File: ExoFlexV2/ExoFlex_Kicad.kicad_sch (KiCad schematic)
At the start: 25 parts, among them J1 ScrewT+12V, J19 CN9, J2 ScrewT5V, J20 CN10, J3 ScrewTGND, J4 ScrewT12V, J5 ScrewT-12v, J6 CN7, J7 CN8, M1 MOT_EV(12V 9.2A), M2 MOT_DOR(12V 9.2A), P1 Conn_WallPlug, U2 ON/OFF_SW(20A), U3 SECU_BUT(20A)

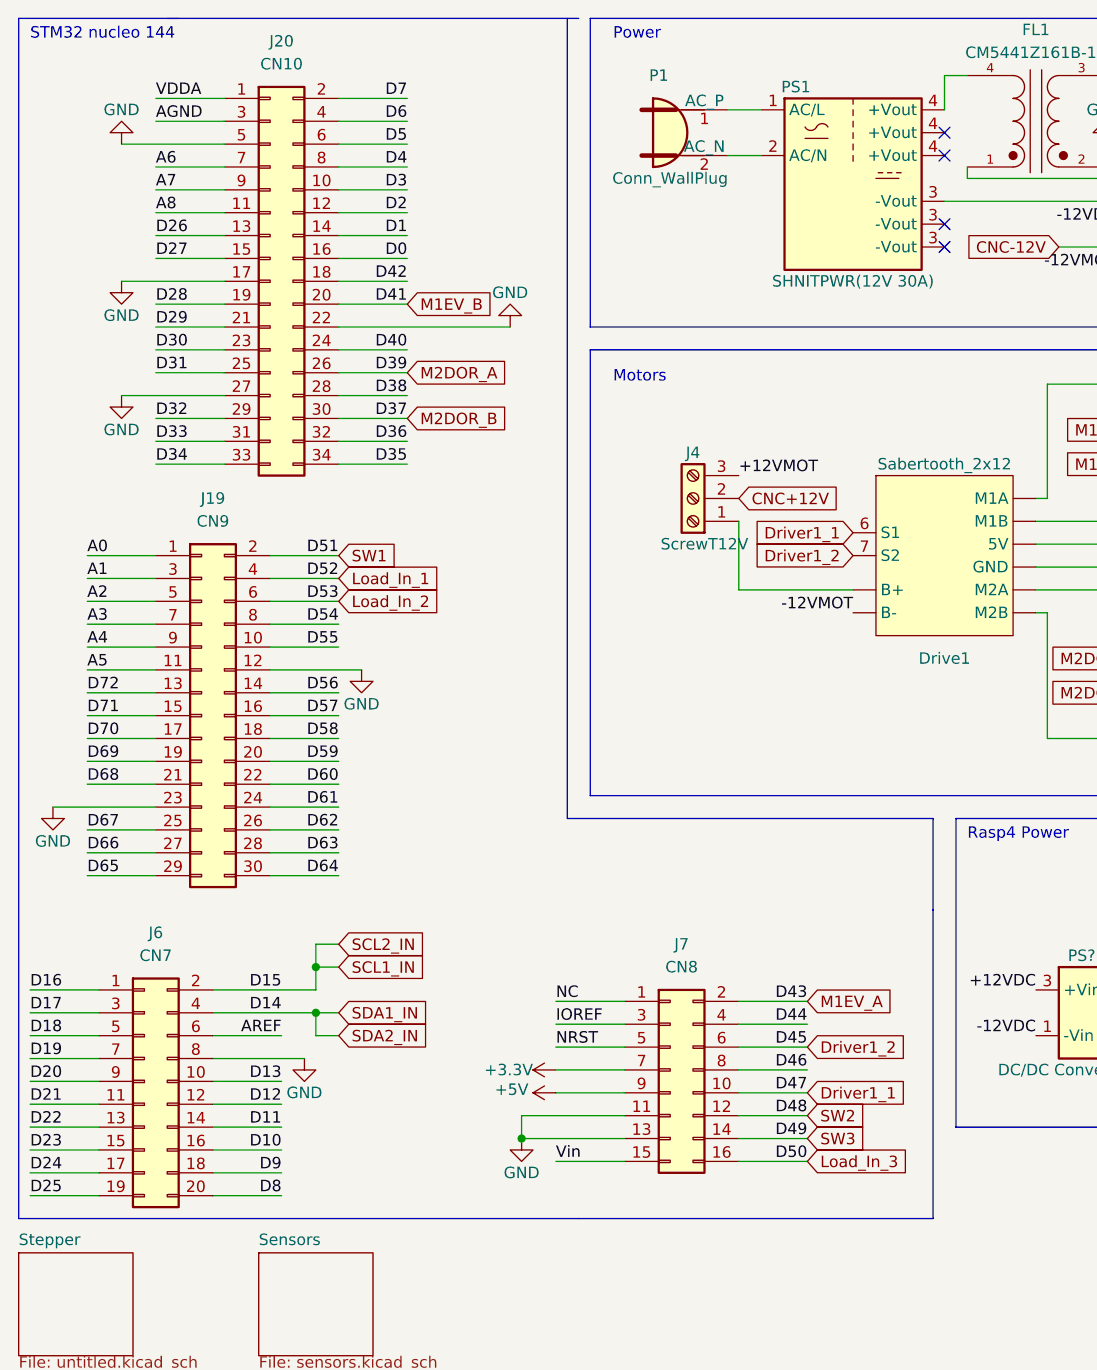
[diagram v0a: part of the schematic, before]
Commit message: Ajout des capteurs de courant, loadcell et potentiomètre et remplacement du stm32 par Raspberry Pi 4
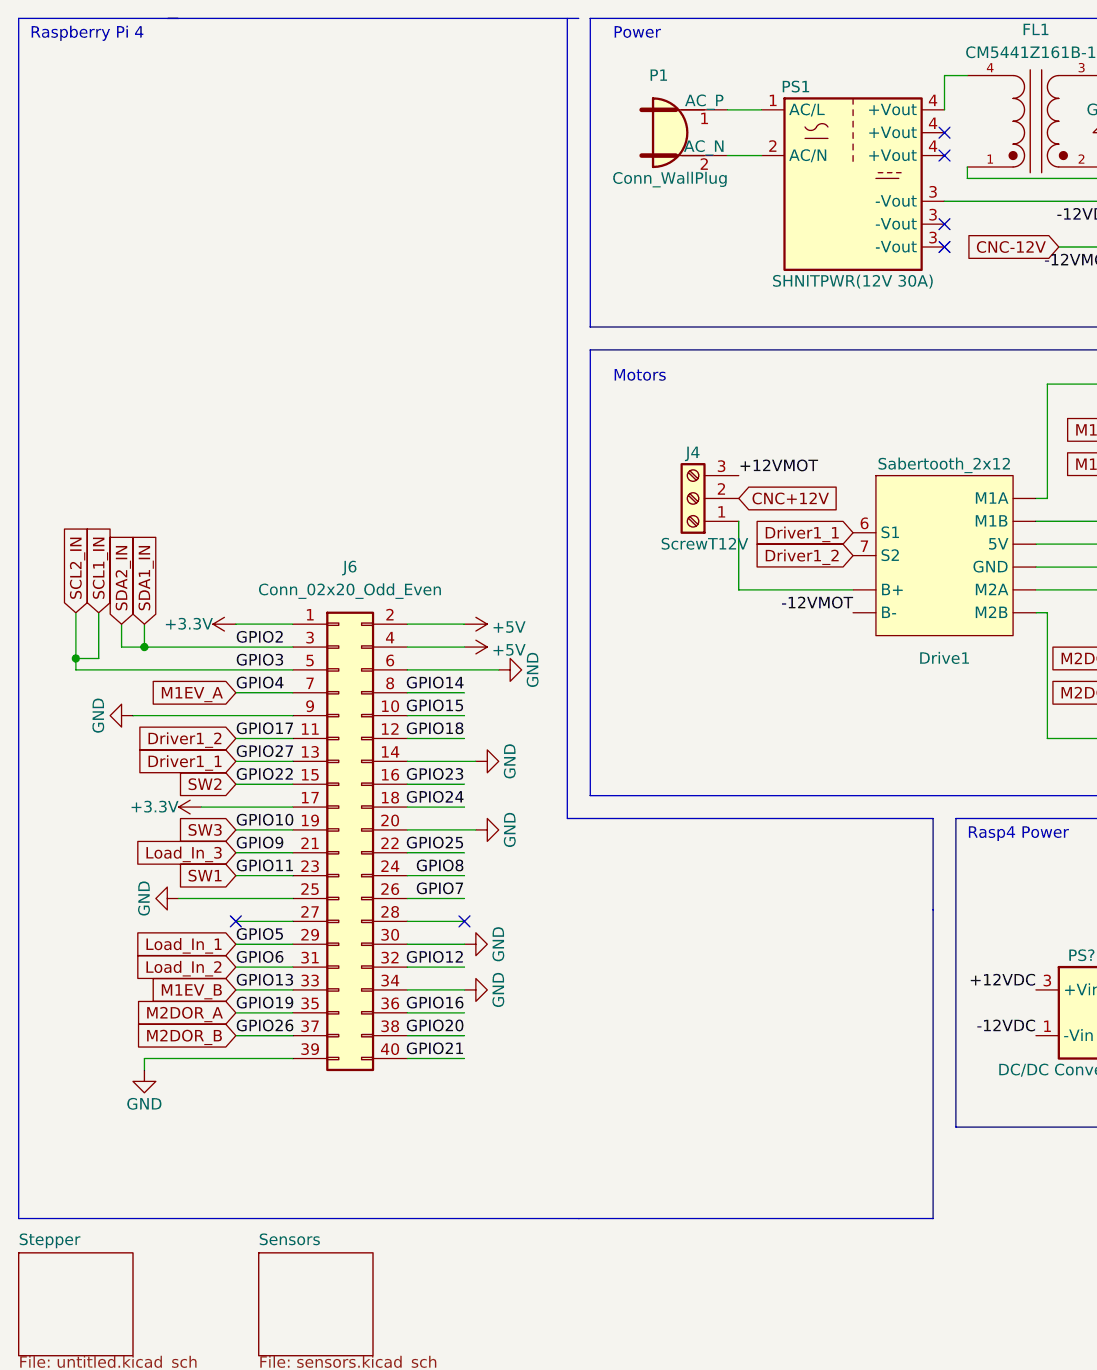
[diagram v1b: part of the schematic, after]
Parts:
- removed J19: CN9, Connector_PinSocket_2.54mm:PinSocket_2x15_P2.54mm_Vertical, symbol Connector_Generic:Conn_02x15_Odd_Even
- removed J20: CN10, Connector_PinSocket_2.54mm:PinSocket_2x17_P2.54mm_Vertical, symbol Connector_Generic:Conn_02x17_Odd_Even
- removed J6: CN7, Connector_PinSocket_2.54mm:PinSocket_2x10_P2.54mm_Vertical, symbol Connector_Generic:Conn_02x10_Odd_Even
- removed J7: CN8, Connector_PinSocket_2.54mm:PinSocket_2x08_P2.54mm_Vertical, symbol Connector_Generic:Conn_02x08_Odd_Even
- added J6: Conn_02x20_Odd_Even, symbol Connector_Generic:Conn_02x20_Odd_Even
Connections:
- net +3V3: now also J6.1 (Pin_1), J6.17 (Pin_17)
- net +5V: now also J6.2 (Pin_2), J6.4 (Pin_4)
- net Driver1_1: now also J6.13 (Pin_13)
- net Driver1_2: now also J6.11 (Pin_11)
- net GND: now also J6.14 (Pin_14), J6.20 (Pin_20), J6.25 (Pin_25), J6.30 (Pin_30), J6.34 (Pin_34), J6.39 (Pin_39), J6.6 (Pin_6), J6.9 (Pin_9)
- net Load_In_1: now also J6.29 (Pin_29)
- net Load_In_2: now also J6.31 (Pin_31)
- net Load_In_3: now also J6.21 (Pin_21)
- net M1EV_A: now also J6.7 (Pin_7)
- net M1EV_B: now also J6.33 (Pin_33)
- net M2DOR_A: now also J6.35 (Pin_35)
- net M2DOR_B: now also J6.37 (Pin_37)
- net SCL1_IN: now also J6.5 (Pin_5)
- net SDA1_IN: now also J6.3 (Pin_3)
- net SW1: now also J6.23 (Pin_23)
- net SW2: now also J6.15 (Pin_15)
- net SW3: now also J6.19 (Pin_19)
- net at PS1.3 (-Vout): now also J5.1 (Pin_1)
- net at PS1.4 (+Vout): now also FL1.4
- net at P?.S1 (Data_1): now also U?.3
- net at P?.S2 (Data_2): now also PS?.4 (-Vout)
- new net GPIO12: J6.32 (Pin_32)
- new net GPIO14: J6.8 (Pin_8)
- new net GPIO15: J6.10 (Pin_10)
- new net GPIO16: J6.36 (Pin_36)
- new net GPIO18: J6.12 (Pin_12)
- new net GPIO20: J6.38 (Pin_38)
- new net GPIO21: J6.40 (Pin_40)
- new net GPIO23: J6.16 (Pin_16)
- new net GPIO24: J6.18 (Pin_18)
- new net GPIO25: J6.22 (Pin_22)
- new net GPIO7: J6.26 (Pin_26)
- new net GPIO8: J6.24 (Pin_24)
- no-connect marks 8 -> 10
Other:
- note added: "Raspberry Pi 4"
- note removed: "STM32 nucleo 144"

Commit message: Backup du stm32
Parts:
- added J19: CN9, Connector_PinSocket_2.54mm:PinSocket_2x15_P2.54mm_Vertical, symbol Connector_Generic:Conn_02x15_Odd_Even
- added J20: CN10, Connector_PinSocket_2.54mm:PinSocket_2x17_P2.54mm_Vertical, symbol Connector_Generic:Conn_02x17_Odd_Even
- added J6: CN7, Connector_PinSocket_2.54mm:PinSocket_2x10_P2.54mm_Vertical, symbol Connector_Generic:Conn_02x10_Odd_Even
- added J7: CN8, Connector_PinSocket_2.54mm:PinSocket_2x08_P2.54mm_Vertical, symbol Connector_Generic:Conn_02x08_Odd_Even
- renumbered J6 to J21
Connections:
- net +3V3: now also J7.7 (Pin_7)
- net +5V: now also J7.9 (Pin_9)
- net Driver1_1: now also J7.10 (Pin_10); no longer J21.13 (Pin_13)
- net Driver1_2: now also J7.6 (Pin_6); no longer J21.11 (Pin_11)
- net GND: now also J19.12 (Pin_12), J19.23 (Pin_23), J20.17 (Pin_17), J20.22 (Pin_22), J20.27 (Pin_27), J20.5 (Pin_5), J6.8 (Pin_8), J7.11 (Pin_11), J7.13 (Pin_13)
- net Load_In_1: now also J19.4 (Pin_4); no longer J21.29 (Pin_29)
- net Load_In_2: now also J19.6 (Pin_6); no longer J21.31 (Pin_31)
- net Load_In_3: now also J7.16 (Pin_16); no longer J21.21 (Pin_21)
- net M1EV_A: now also J7.2 (Pin_2); no longer J21.7 (Pin_7)
- net M1EV_B: now also J20.20 (Pin_20); no longer J21.33 (Pin_33)
- net M2DOR_A: now also J20.26 (Pin_26); no longer J21.35 (Pin_35)
- net M2DOR_B: now also J20.30 (Pin_30); no longer J21.37 (Pin_37)
- net SCL1_IN: now also J6.2 (Pin_2); no longer J21.5 (Pin_5)
- net SDA1_IN: now also J6.4 (Pin_4); no longer J21.3 (Pin_3)
- net SW1: now also J19.2 (Pin_2); no longer J21.23 (Pin_23)
- net SW2: now also J7.12 (Pin_12); no longer J21.15 (Pin_15)
- net SW3: now also J7.14 (Pin_14); no longer J21.19 (Pin_19)
- net at PS1.3 (-Vout): now also J5.1 (Pin_1)
- net at PS1.4 (+Vout): now also FL1.4
- net at P?.S1 (Data_1): now also U?.3
- net at P?.S2 (Data_2): now also PS?.4 (-Vout)
- new net A0: J19.1 (Pin_1)
- new net A1: J19.3 (Pin_3)
- new net A2: J19.5 (Pin_5)
- new net A3: J19.7 (Pin_7)
- new net A4: J19.9 (Pin_9)
- new net A5: J19.11 (Pin_11)
- new net A6: J20.7 (Pin_7)
- new net A7: J20.9 (Pin_9)
- new net A8: J20.11 (Pin_11)
- new net AGND: J20.3 (Pin_3)
- new net AREF: J6.6 (Pin_6)
- new net D0: J20.16 (Pin_16)
- new net D1: J20.14 (Pin_14)
- new net D10: J6.16 (Pin_16)
- new net D11: J6.14 (Pin_14)
- new net D12: J6.12 (Pin_12)
- new net D13: J6.10 (Pin_10)
- new net D16: J6.1 (Pin_1)
- new net D17: J6.3 (Pin_3)
- new net D18: J6.5 (Pin_5)
- new net D19: J6.7 (Pin_7)
- new net D2: J20.12 (Pin_12)
- new net D20: J6.9 (Pin_9)
- new net D21: J6.11 (Pin_11)
- new net D22: J6.13 (Pin_13)
- new net D23: J6.15 (Pin_15)
- new net D24: J6.17 (Pin_17)
- new net D25: J6.19 (Pin_19)
- new net D26: J20.13 (Pin_13)
- new net D27: J20.15 (Pin_15)
- new net D28: J20.19 (Pin_19)
- new net D29: J20.21 (Pin_21)
- new net D3: J20.10 (Pin_10)
- new net D30: J20.23 (Pin_23)
- new net D31: J20.25 (Pin_25)
- new net D32: J20.29 (Pin_29)
- new net D33: J20.31 (Pin_31)
- new net D34: J20.33 (Pin_33)
- new net D35: J20.34 (Pin_34)
- new net D36: J20.32 (Pin_32)
- new net D38: J20.28 (Pin_28)
- new net D4: J20.8 (Pin_8)
- new net D40: J20.24 (Pin_24)
- new net D42: J20.18 (Pin_18)
- new net D44: J7.4 (Pin_4)
- new net D46: J7.8 (Pin_8)
- new net D5: J20.6 (Pin_6)
- new net D54: J19.8 (Pin_8)
- new net D55: J19.10 (Pin_10)
- new net D56: J19.14 (Pin_14)
- new net D57: J19.16 (Pin_16)
- new net D58: J19.18 (Pin_18)
- new net D59: J19.20 (Pin_20)
- new net D6: J20.4 (Pin_4)
- new net D60: J19.22 (Pin_22)
- new net D61: J19.24 (Pin_24)
- new net D62: J19.26 (Pin_26)
- new net D63: J19.28 (Pin_28)
- new net D64: J19.30 (Pin_30)
- new net D65: J19.29 (Pin_29)
- new net D66: J19.27 (Pin_27)
- new net D67: J19.25 (Pin_25)
- new net D68: J19.21 (Pin_21)
- new net D69: J19.19 (Pin_19)
- new net D7: J20.2 (Pin_2)
- new net D70: J19.17 (Pin_17)
- new net D71: J19.15 (Pin_15)
- new net D8: J6.20 (Pin_20)
- new net D9: J6.18 (Pin_18)
- new net GPIO10: J21.19 (Pin_19)
- new net GPIO11: J21.23 (Pin_23)
- new net GPIO13: J21.33 (Pin_33)
- new net GPIO17: J21.11 (Pin_11)
- new net GPIO19: J21.35 (Pin_35)
- new net GPIO2: J21.3 (Pin_3)
- new net GPIO22: J21.15 (Pin_15)
- new net GPIO26: J21.37 (Pin_37)
- new net GPIO27: J21.13 (Pin_13)
- new net GPIO3: J21.5 (Pin_5)
- new net GPIO4: J21.7 (Pin_7)
- new net GPIO5: J21.29 (Pin_29)
- new net GPIO6: J21.31 (Pin_31)
- new net GPIO9: J21.21 (Pin_21)
- new net IOREF: J7.3 (Pin_3)
- new net NC: J7.1 (Pin_1)
- new net NRST: J7.5 (Pin_5)
- new net VDDA: J20.1 (Pin_1)
- new net Vin: J7.15 (Pin_15)
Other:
- note added: "Raspberry pi 4"
- note added: "STM32 nucleo 144"
- note removed: "Raspberry Pi 4"
- moved on the sheet: J21

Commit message: Plein de modification
Beaucoup trop pour que le commit soit intéressant
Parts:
- removed C1: 220uF 16V, symbol Device:C_Polarized_US
- removed D1: 5.0SMDJ12CA, symbol Device:D_Zener
- removed D2: MBRB4030T4G, symbol Device:D_Zener
- removed Drive1: Sabertooth_2x12, symbol Driver_Motor:Sabertooth_2x12
- removed F1: Fuse_20A, symbol Device:Fuse
- removed FL1: CM5441Z161B-10, FIL_CM5441Z161B-10, symbol CM5441Z161B-10:CM5441Z161B-10
- removed J1: ScrewT+12V, symbol Connector:Screw_Terminal_01x03
- removed J19: CN9, Connector_PinSocket_2.54mm:PinSocket_2x15_P2.54mm_Vertical, symbol Connector_Generic:Conn_02x15_Odd_Even
- removed J2: ScrewT5V, symbol Connector:Screw_Terminal_01x03
- removed J20: CN10, Connector_PinSocket_2.54mm:PinSocket_2x17_P2.54mm_Vertical, symbol Connector_Generic:Conn_02x17_Odd_Even
- removed J21: Conn_02x20_Odd_Even, symbol Connector_Generic:Conn_02x20_Odd_Even
- removed J3: ScrewTGND, symbol Connector:Screw_Terminal_01x03
- removed J4: ScrewT12V, symbol Connector:Screw_Terminal_01x03
- removed J5: ScrewT-12v, symbol Connector:Screw_Terminal_01x04
- removed J6: CN7, Connector_PinSocket_2.54mm:PinSocket_2x10_P2.54mm_Vertical, symbol Connector_Generic:Conn_02x10_Odd_Even
- removed J7: CN8, Connector_PinSocket_2.54mm:PinSocket_2x08_P2.54mm_Vertical, symbol Connector_Generic:Conn_02x08_Odd_Even
- removed M1: MOT_EV(12V 9.2A), symbol Motor:Motor_DC
- removed M2: MOT_DOR(12V 9.2A), symbol Motor:Motor_DC
- removed P1: Conn_WallPlug, symbol Connector:Conn_WallPlug
- removed P?: USB_C_Plug, symbol Connector:USB_C_Plug
- removed PS1: SHNITPWR(12V 30A), Converter_ACDC:Converter_ACDC_HiLink_HLK-PMxx, symbol Converter_ACDC:HLK-PM01
- removed PS?: DC/DC Converter (12V-5.1V 10A), Converter_DCDC:Converter_DCDC_XP_POWER-IAxxxxD_THT, symbol Converter_DCDC:IA0305D
- removed U2: ON/OFF_SW(20A), Package_SO:SOIC-16_3.9x9.9mm_P1.27mm, symbol Analog_Switch:DG308AxY
- removed U3: SECU_BUT(20A), Package_SO:SOIC-16_3.9x9.9mm_P1.27mm, symbol Analog_Switch:DG308AxY
- removed U?: Raspberry_Pi_4 (5.1V 3A), symbol Connector:Raspberry_Pi_4
- removed U?: Switch(3A), Package_SO:SOIC-16_3.9x9.9mm_P1.27mm, symbol Analog_Switch:DG308AxY
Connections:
- no-connect marks 10 -> 0
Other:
- sheet Sensors renamed LIMIT SWITCH                                                                                                        8
- removed sheet Stepper
- added sheet BLOCK DIAGRAM                                                                                                     2 (blockdiagram.kicad_sch)
- added sheet LOAD CELLS                                                                                                         7 (loadcells.kicad_sch)
- added sheet MAGNETIC ENCODER                                                                                                 6 (magneticencoder.kicad_sch)
- added sheet MOTOR ENCODER                                                                                                    5 (motors.kicad_sch)
- added sheet OTHER SENSORS                                                                                                    10 (currentsensors.kicad_sch)
- added sheet POWER                                                                                                              3 (power.kicad_sch)
- added sheet PROXIMITY SENSORS                                                                                                 9                                                                                        (proximitysensors.kicad_sch)
- added sheet STM SIGNALS                                                                                                        4 (stmsignal.kicad_sch)
- note added: "BUMBLEBEE"
- note added: "EXOFLEX SHIELD"
- note added: "RÉVISION 1.00 DATE : 15 JANVIER 2024"
- note removed: "* Indicates a PWM-capable pin"
- note removed: "Arduino Serial(5V)"
- note removed: "Motors"
- note removed: "Power"
- note removed: "Rasp4 Power"
- note removed: "Raspberry pi 4"
- note removed: "STM32 nucleo 144"
- company: (none) -> ExoFlex
- title: ExoFlex Electric Schematic -> BUMBLEBEE
